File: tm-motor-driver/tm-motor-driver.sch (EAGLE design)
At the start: 18 parts

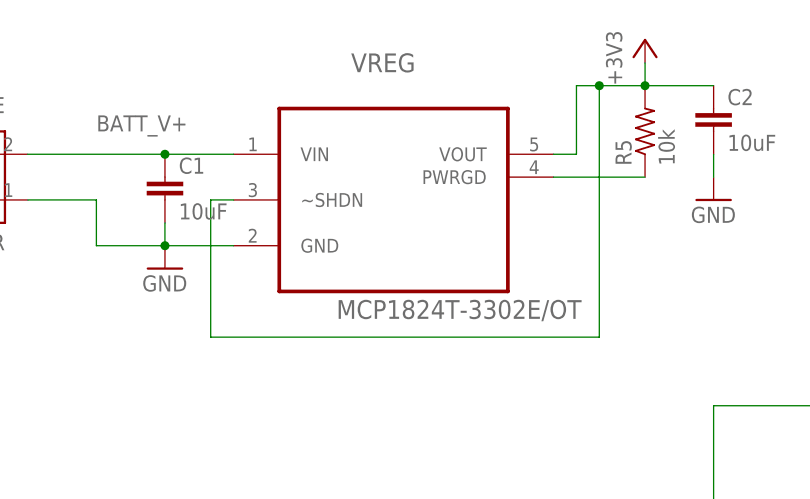
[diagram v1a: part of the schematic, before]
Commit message: Fix power supply, shutdown should be connected to Vin not Vout
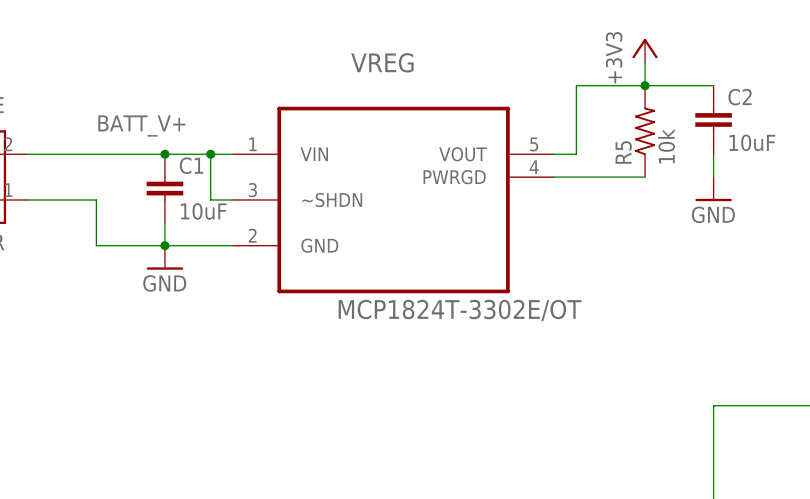
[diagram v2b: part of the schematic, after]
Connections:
- net +3V3: no longer VREG.~SHDN
- net BATT_V+: now also VREG.~SHDN
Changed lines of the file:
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@@
 <label x="30.48" y="154.94" size="1.778" layer="95"/>
 <pinref part="C1" gate="G$1" pin="1"/>
-<wire x1="38.1" y1="152.4" x2="45.72" y2="152.4" width="0.1524" layer="91"/>
+<wire x1="38.1" y1="152.4" x2="43.18" y2="152.4" width="0.1524" layer="91"/>
 <pinref part="POWER" gate="G$1" pin="2"/>
+<wire x1="43.18" y1="152.4" x2="45.72" y2="152.4" width="0.1524" layer="91"/>
 <wire x1="38.1" y1="152.4" x2="22.86" y2="152.4" width="0.1524" layer="91"/>
 <junction x="38.1" y="152.4"/>
+<pinref part="VREG" gate="A" pin="~SHDN"/>
+<wire x1="45.72" y1="147.32" x2="43.18" y2="147.32" width="0.1524" layer="91"/>
+<wire x1="43.18" y1="147.32" x2="43.18" y2="152.4" width="0.1524" layer="91"/>
+<junction x="43.18" y="152.4"/>
 </segment>
 </net>
@@
 <wire x1="81.28" y1="152.4" x2="83.82" y2="152.4" width="0.1524" layer="91"/>
 <wire x1="83.82" y1="152.4" x2="83.82" y2="160.02" width="0.1524" layer="91"/>
-<wire x1="83.82" y1="160.02" x2="86.36" y2="160.02" width="0.1524" layer="91"/>
 <junction x="91.44" y="160.02"/>
 <pinref part="C2" gate="G$1" pin="1"/>
-<wire x1="86.36" y1="160.02" x2="91.44" y2="160.02" width="0.1524" layer="91"/>
+<wire x1="83.82" y1="160.02" x2="91.44" y2="160.02" width="0.1524" layer="91"/>
 <wire x1="99.06" y1="160.02" x2="91.44" y2="160.02" width="0.1524" layer="91"/>
-<pinref part="VREG" gate="A" pin="~SHDN"/>
-<wire x1="45.72" y1="147.32" x2="43.18" y2="147.32" width="0.1524" layer="91"/>
-<wire x1="43.18" y1="147.32" x2="43.18" y2="132.08" width="0.1524" layer="91"/>
-<wire x1="43.18" y1="132.08" x2="86.36" y2="132.08" width="0.1524" layer="91"/>
-<wire x1="86.36" y1="132.08" x2="86.36" y2="160.02" width="0.1524" layer="91"/>
-<junction x="86.36" y="160.02"/>
 </segment>
 </net>
